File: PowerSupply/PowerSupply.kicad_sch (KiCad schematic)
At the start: 21 parts, among them J1 AC+, J2 AC-, J3 POWER, U1 LM317_SOT-223, U2 LM337_SOT223

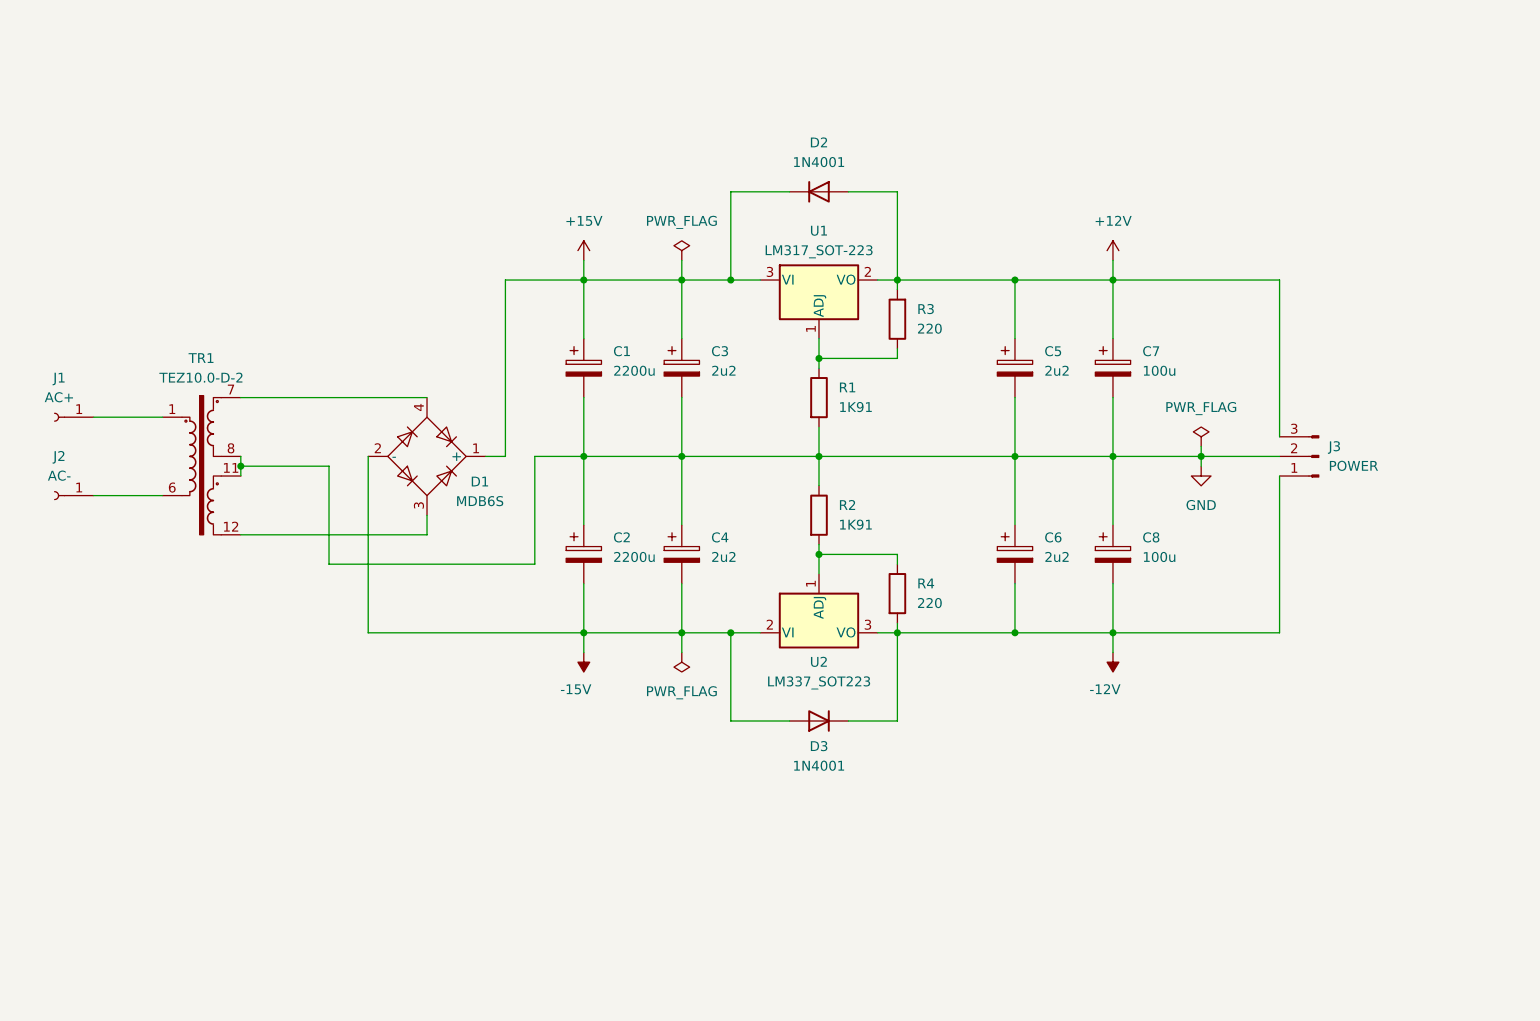
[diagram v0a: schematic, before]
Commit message: Power Supply Board
Updated the power supply schematic.
Updated the power supply board.
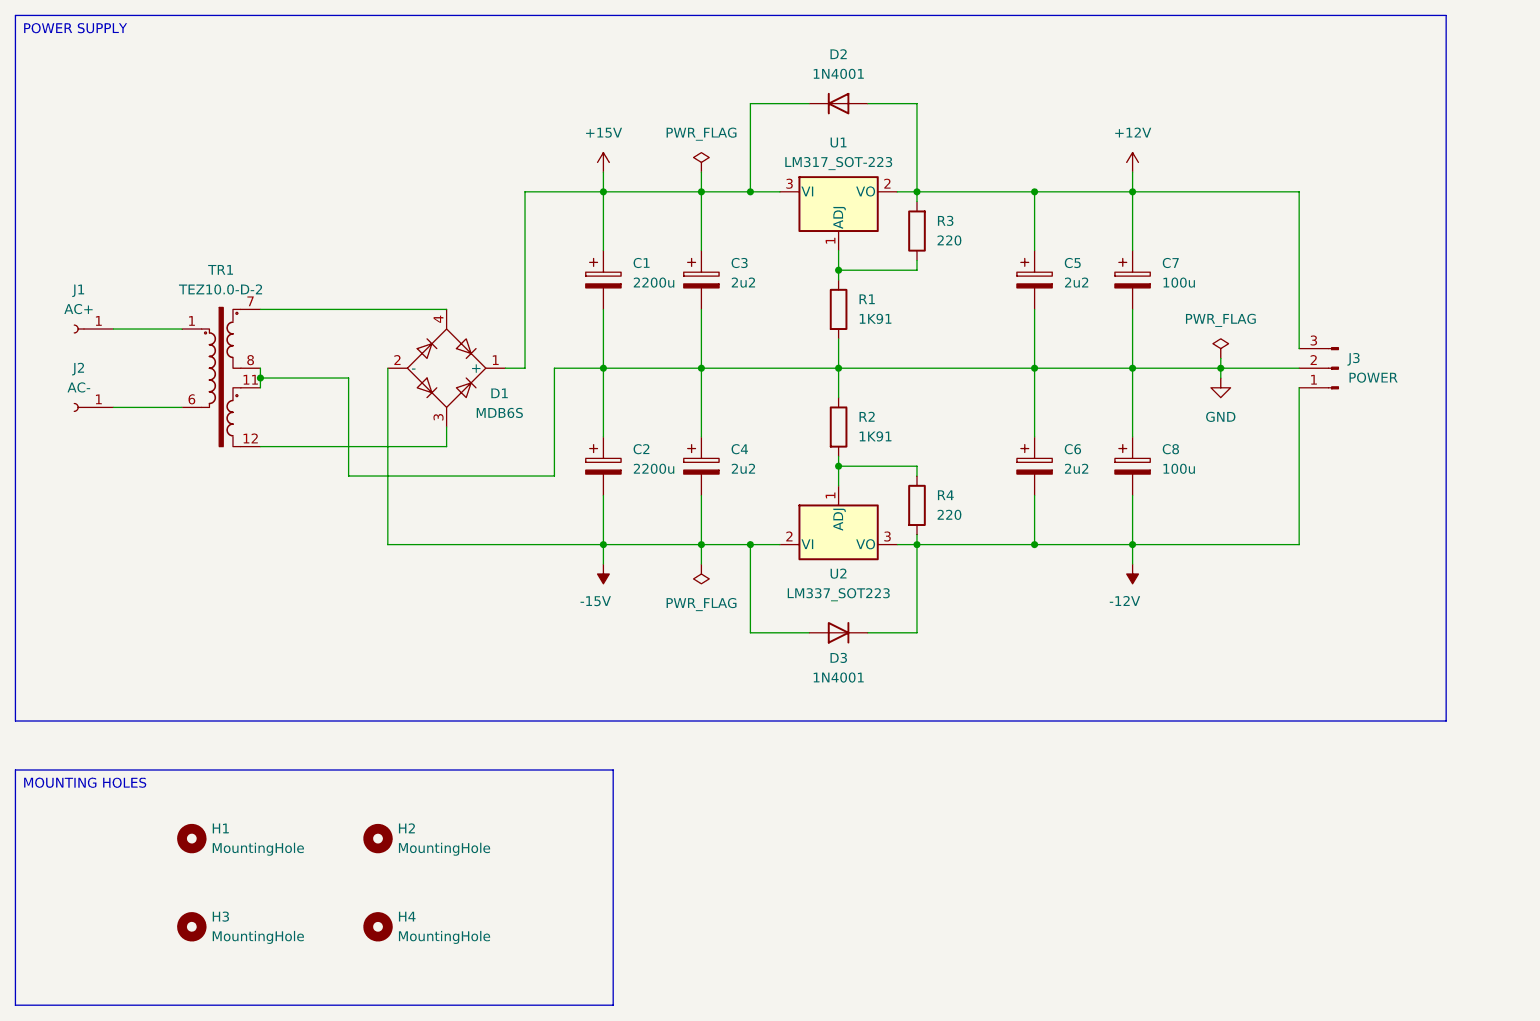
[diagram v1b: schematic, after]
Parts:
- added H1, H2, H3, H4: MountingHole, MountingHole:MountingHole_3.2mm_M3, symbol Mechanical:MountingHole
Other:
- moved on the sheet: C1, C2, C3, C4, C5, C6, C7, C8, D1, D2, D3, J1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

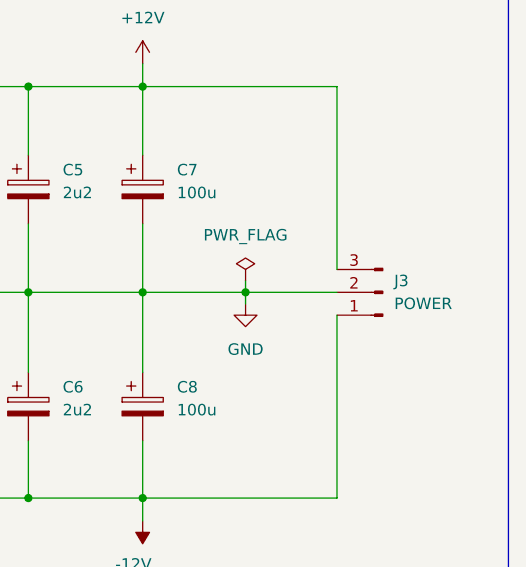
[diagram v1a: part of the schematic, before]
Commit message: Preamplifier Schematic
Added the preamplifier schematic.
Updated the preamplifier project.
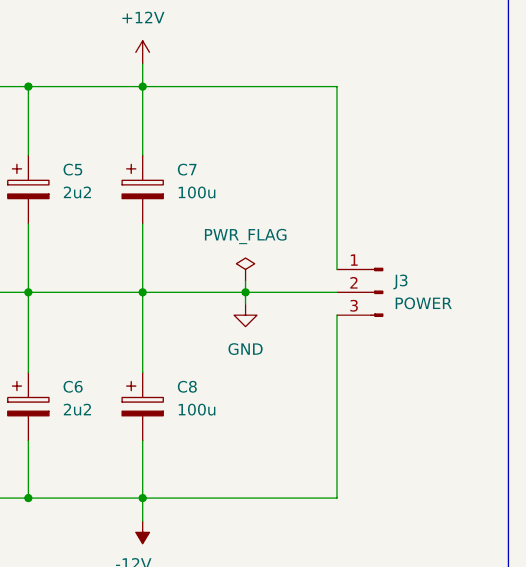
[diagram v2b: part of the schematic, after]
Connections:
- net +12V: now also J3.1 (Pin_1); no longer J3.3 (Pin_3)
- net -12V: now also J3.3 (Pin_3); no longer J3.1 (Pin_1)
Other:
- moved on the sheet: J3
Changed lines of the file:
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@@
 	(symbol
 		(lib_id "Connector:Conn_01x03_Pin")
-		(at 224.79 86.36 180)
+		(at 224.79 86.36 0)
+		(mirror y)
 		(unit 1)
 		(exclude_from_sim no)
@@
 		(on_board yes)
 		(dnp no)
-		(fields_autoplaced yes)
 		(property "Reference" "J3"
-			(at 226.06 85.0899 0)
+			(at 226.06 85.0901 0)
 			(effects
 				(font
@@
 		)
 		(property "Value" "POWER"
-			(at 226.06 87.6299 0)
+			(at 226.06 87.6301 0)
 			(effects
 				(font

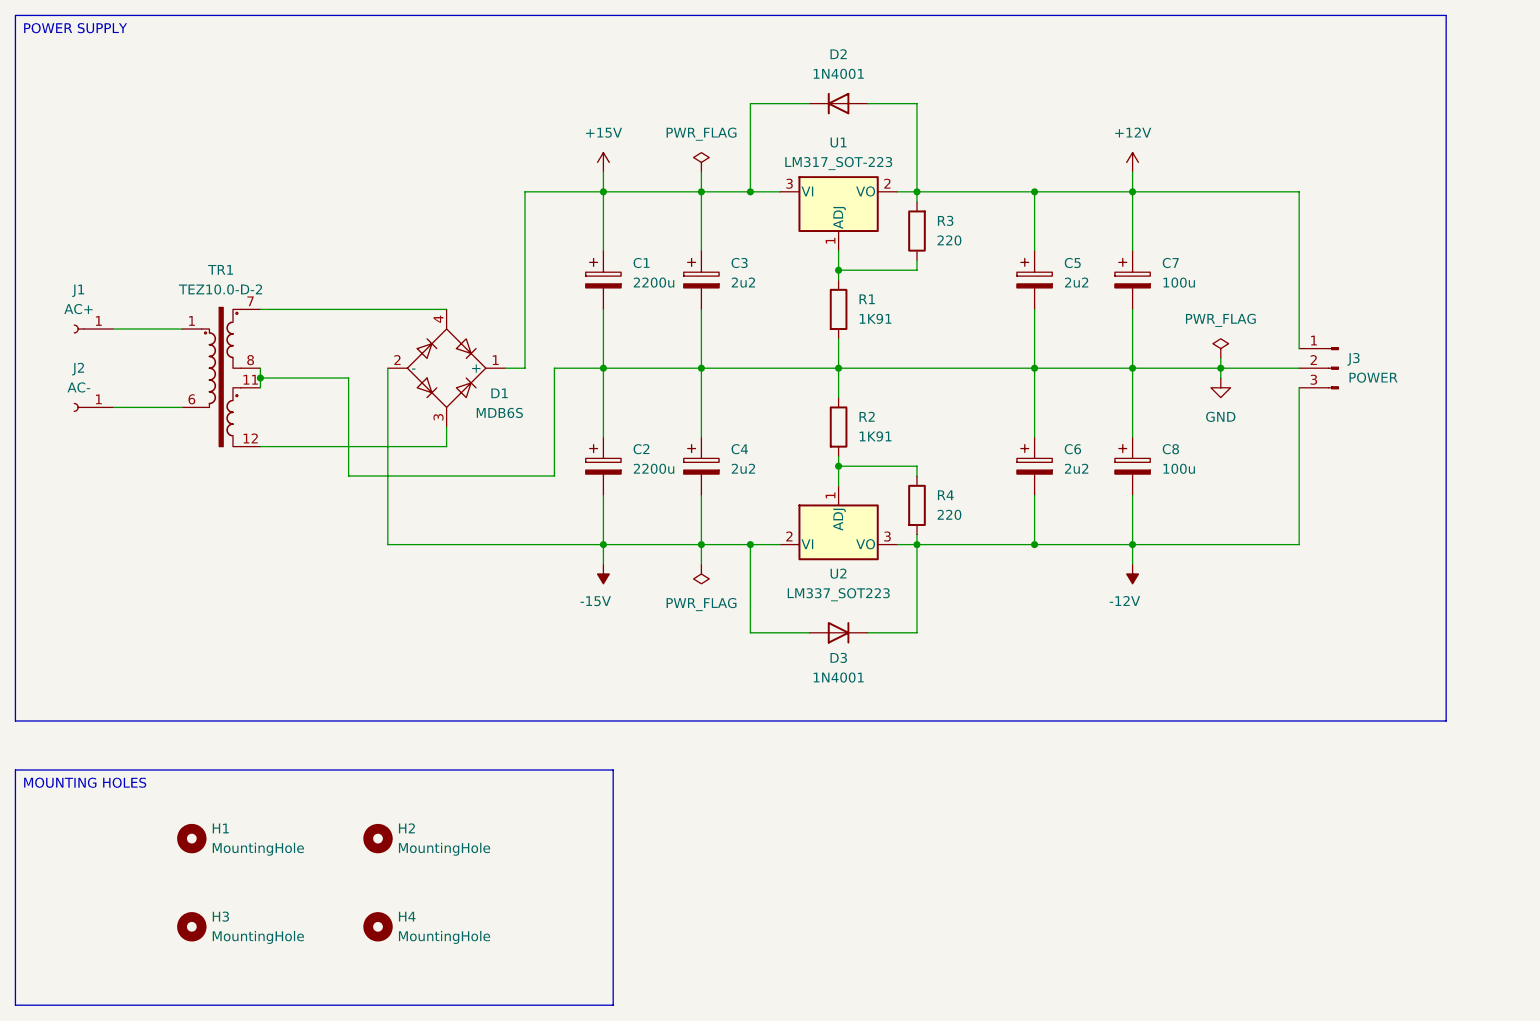
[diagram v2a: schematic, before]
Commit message: Power Supply Board
Updated the power supply board design.
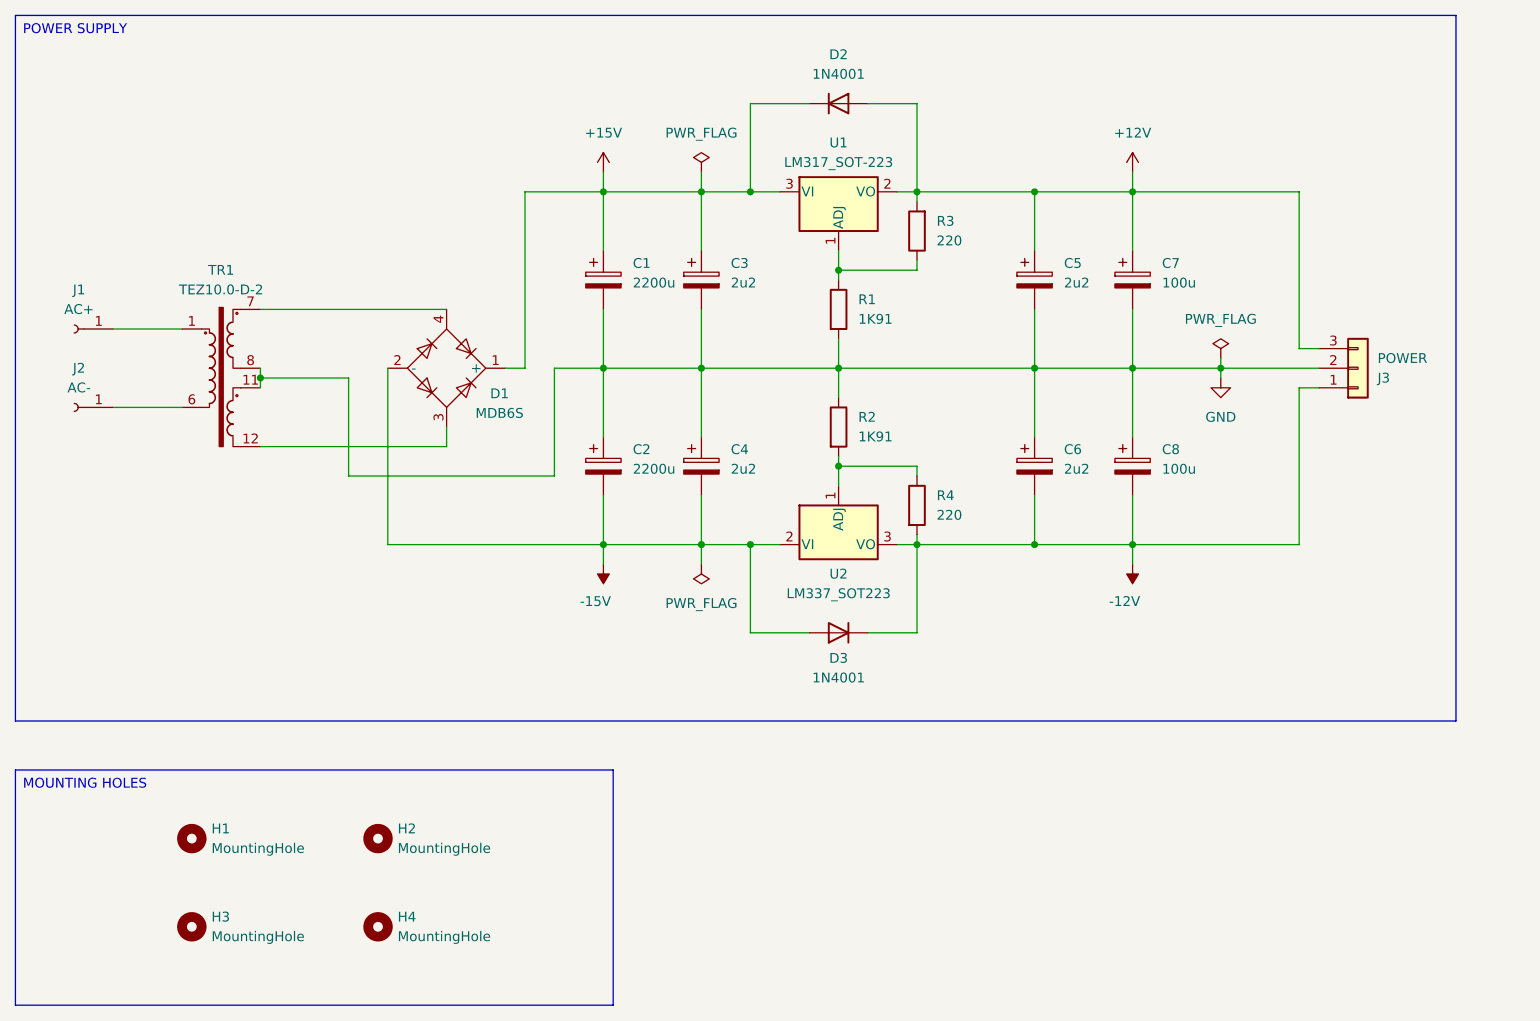
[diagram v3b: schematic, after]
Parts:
- removed J3: POWER, Connector_Molex:Molex_KK-254_AE-6410-03A_1x03_P2.54mm_Vertical, symbol Connector:Conn_01x03_Pin
- added J3: POWER, Custom_Parts:Molex_KK-254_1x03_P2.54mm_Vertical, symbol Connector_Generic:Conn_01x03
- TR1: footprint Transformer_THT:Transformer_Breve_TEZ-44x52 -> Custom_Parts:TRANSFORMER_TEZ-44X52
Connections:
- net +12V: now also J3.3 (Pin_3)
- net -12V: now also J3.1 (Pin_1)
- net GND: now also J3.2 (Pin_2)
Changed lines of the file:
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@@
 		(exclude_from_sim no)
 		(at 53.34 40.64 0)
-		(size 185.42 91.44)
+		(size 186.69 91.44)
 		(margins 0.9525 0.9525 0.9525 0.9525)
 		(stroke
@@
 	(wire
 		(pts
-			(xy 209.55 86.36) (xy 219.71 86.36)
+			(xy 209.55 86.36) (xy 222.25 86.36)
 		)
 		(stroke
@@
 	(wire
 		(pts
+			(xy 219.71 83.82) (xy 222.25 83.82)
+		)
+		(stroke
+			(width 0)
+			(type default)
+		)
+	)
+	(wire
+		(pts
 			(xy 198.12 86.36) (xy 198.12 95.25)
 		)
@@
 	(wire
 		(pts
+			(xy 219.71 88.9) (xy 222.25 88.9)
+		)
+		(stroke
+			(width 0)
+			(type default)
+		)
+	)
+	(wire
+		(pts
 			(xy 129.54 60.96) (xy 129.54 63.5)
 		)
@@
 	)
 	(symbol
-		(lib_id "Connector:Conn_01x03_Pin")
-		(at 224.79 86.36 0)
-		(mirror y)
-		(unit 1)
-		(exclude_from_sim no)
-		(in_bom yes)
-		(on_board yes)
-		(dnp no)
-		(property "Reference" "J3"
-			(at 226.06 85.0901 0)
-			(effects
-				(font
-					(size 1.27 1.27)
-				)
-				(justify right)
-			)
-		)
-		(property "Value" "POWER"
-			(at 226.06 87.6301 0)
-			(effects
-				(font
-					(size 1.27 1.27)
-				)
-				(justify right)
-			)
-		)
-		(property "Footprint" "Connector_Molex:Molex_KK-254_AE-6410-03A_1x03_P2.54mm_Vertical"
-			(at 224.79 86.36 0)
-			(effects
-				(font
-					(size 1.27 1.27)
-				)
-				(hide yes)
-			)
-		)
-		(property "Datasheet" "~"
-			(at 224.79 86.36 0)
-			(effects
-				(font
-					(size 1.27 1.27)
-				)
-				(hide yes)
-			)
-		)
-		(property "Description" "Generic connector, single row, 01x03, script generated"
-			(at 224.79 86.36 0)
-			(effects
-				(font
-					(size 1.27 1.27)
-				)
-				(hide yes)
-			)
-		)
-		(pin "3"
-		)
-		(pin "1"
-		)
-		(pin "2"
-		)
-		(instances
-			(project "PowerSupply"
-				(path "/a799d94b-b267-47a5-8906-3cd7dbbcc515"
-					(reference "J3")
-					(unit 1)
-				)
-			)
-		)
-	)
-	(symbol
 		(lib_id "Regulator_Linear:LM337_SOT223")
 		(at 160.02 109.22 0)
@@
 			)
 		)
-		(property "Footprint" "Transformer_THT:Transformer_Breve_TEZ-44x52"
+		(property "Footprint" "Custom_Parts:TRANSFORMER_TEZ-44X52"
 			(at 80.01 100.33 0)
 			(effects
@@
 					(unit 1)
 				)
+			)
+		)
+	)
+	(symbol
+		(lib_id "Connector_Generic:Conn_01x03")
+		(at 227.33 86.36 0)
+		(mirror x)
+		(unit 1)
+		(exclude_from_sim no)
+		(in_bom yes)
+		(on_board yes)
+		(dnp no)
+		(property "Reference" "J3"
+			(at 229.87 87.6301 0)
+			(effects
+				(font
+					(size 1.27 1.27)
+				)
+				(justify left)
+			)
+		)
+		(property "Value" "POWER"
+			(at 229.87 85.0901 0)
+			(effects
+				(font
+					(size 1.27 1.27)
+				)
+				(justify left)
+			)
+		)
+		(property "Footprint" "Custom_Parts:Molex_KK-254_1x03_P2.54mm_Vertical"
+			(at 227.33 86.36 0)
+			(effects
+				(font
+					(size 1.27 1.27)
+				)
+				(hide yes)
+			)
+		)
+		(property "Datasheet" "~"
+			(at 227.33 86.36 0)
+			(effects
+				(font
+					(size 1.27 1.27)
+				)
+				(hide yes)
+			)
+		)
+		(property "Description" "Generic connector, single row, 01x03, script generated (kicad-library-utils/schlib/autogen/connector/)"
+			(at 227.33 86.36 0)
+			(effects
+				(font
+					(size 1.27 1.27)
+				)
+				(hide yes)
+			)
+		)
+		(pin "1"
+		)
+		(pin "3"
+		)
+		(pin "2"
+		)
+		(instances
+			(project ""
+				(path "/a799d94b-b267-47a5-8906-3cd7dbbcc515"
+					(reference "J3")
+					(unit 1)
+				)

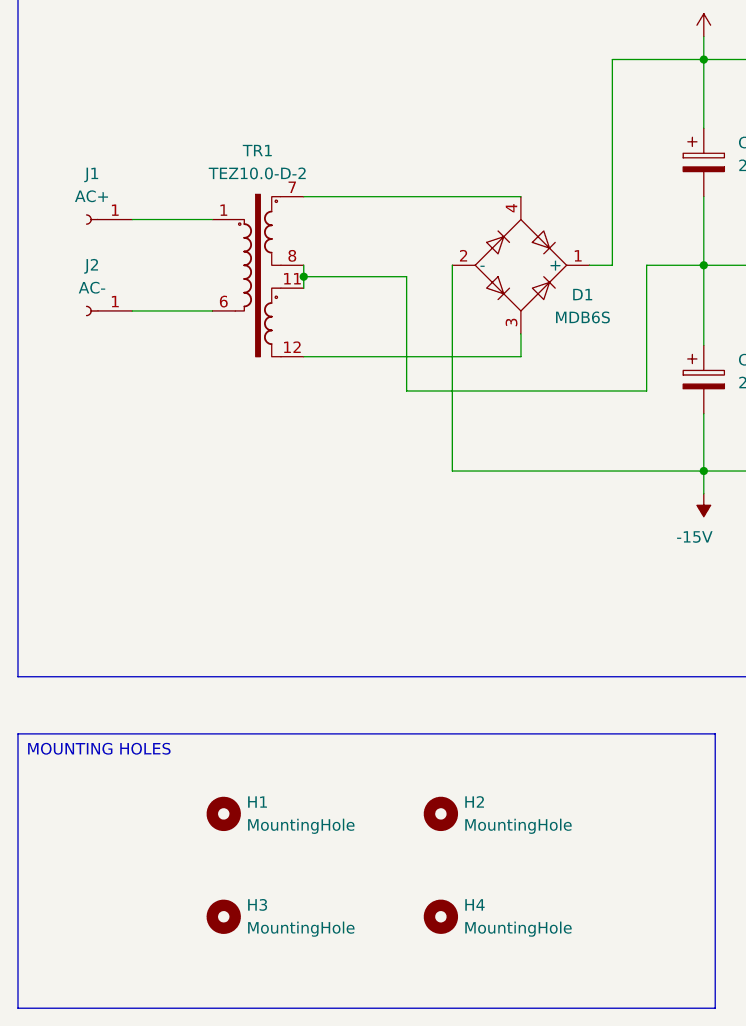
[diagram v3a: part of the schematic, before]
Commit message: Board Designs
Updated the power supply board design.
Updated the preamplifier board design.
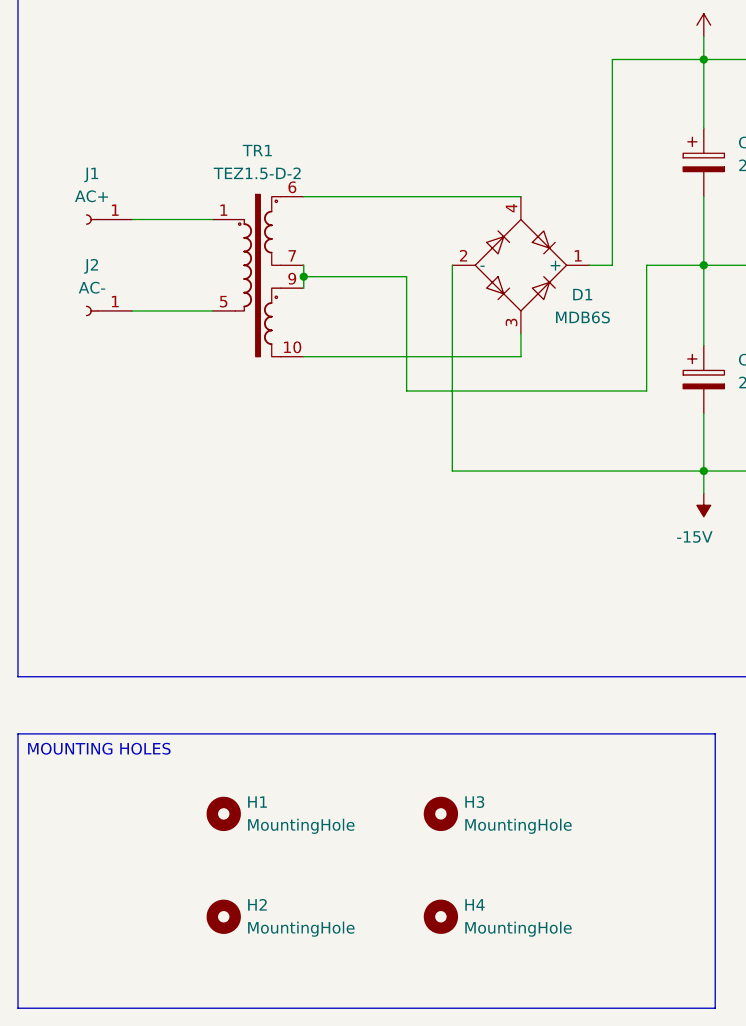
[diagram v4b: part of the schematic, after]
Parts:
- removed TR1: TEZ10.0-D-2, Custom_Parts:TRANSFORMER_TEZ-44X52, symbol Transformer:TEZ10.0-D-2
- added TR1: TEZ1.5-D-2, Custom_Parts:TRANSFORMER_TEZ-35X42, symbol Transformer:TEZ1.5-D-2
- renumbered H3 to H2, H2 to H3
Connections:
- net GND: now also TR1.7, TR1.9
- net at D1.3: now also TR1.10
- net at D1.4: now also TR1.6
- net at J1.1 (Pin_1): now also TR1.1
- net at J2.1 (Pin_1): now also TR1.5
